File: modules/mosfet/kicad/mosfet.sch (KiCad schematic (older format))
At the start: 9 parts, among them P1 CONN_01X02, P2 CONN_01X02, P3 CONN_01X02, P4 CONN_01X02, Q1 BC547, Q2 IRF540N

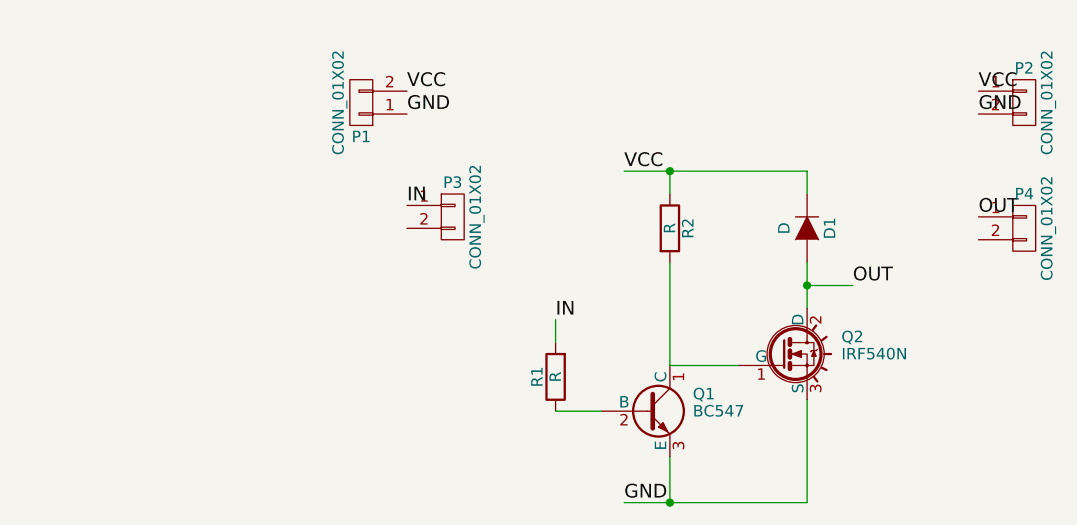
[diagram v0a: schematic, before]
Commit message: Fixes issue #1
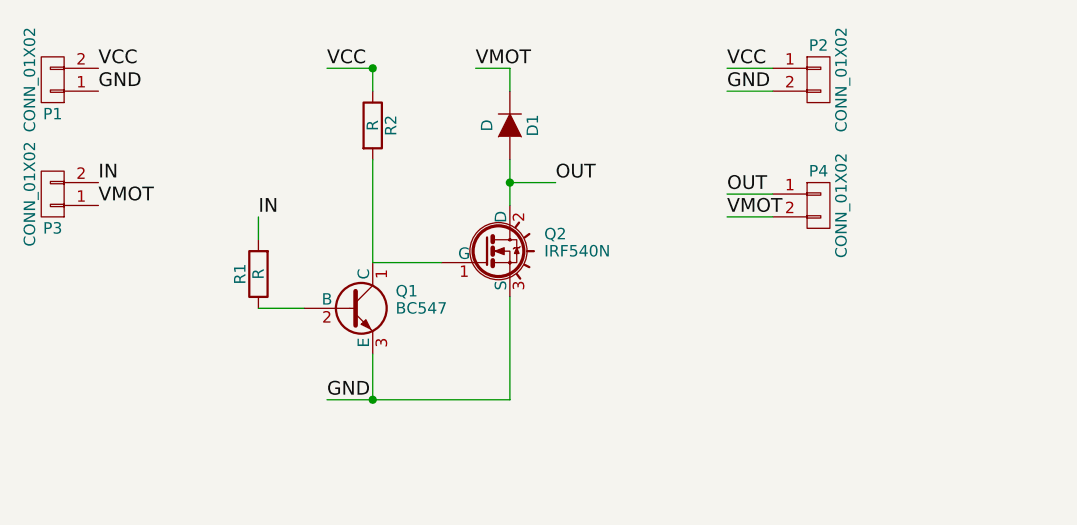
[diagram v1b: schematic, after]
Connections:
- net IN: now also P3.2 (P2); no longer P3.1 (P1)
- net VCC: no longer D1.1 (K)
- net VMOT: now reaches P4.2 (P2)
- net VMOT: now also D1.1 (K), P3.1 (P1)
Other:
- moved on the sheet: D1, P1, P2, P3, P4, Q1, Q2, R1, R2
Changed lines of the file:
@@
 LIBS:contrib
 LIBS:valves
-LIBS:modulo_mosfet-cache
+LIBS:mosfet-cache
 EELAYER 25 0
 EELAYER END
@@
 L IRF540N Q2
 U 1 1 5821F323
-P 4350 2300
-F 0 "Q2" H 4600 2375 50  0000 L CNN
-F 1 "IRF540N" H 4600 2300 50  0000 L CNN
-F 2 "TO_SOT_Packages_THT:TO-220_Neutral123_Vertical_LargePads" H 4600 2225 50  0001 L CIN
-F 3 "" H 4350 2300 50  0000 L CNN
-	1    4350 2300
+P 3050 1850
+F 0 "Q2" H 3300 1925 50  0000 L CNN
+F 1 "IRF540N" H 3300 1850 50  0000 L CNN
+F 2 "TO_SOT_Packages_THT:TO-220_Neutral123_Vertical_LargePads" H 3300 1775 50  0001 L CIN
+F 3 "" H 3050 1850 50  0000 L CNN
+	1    3050 1850
 	1    0    0    -1
 $EndComp
@@
 L BC547 Q1
 U 1 1 5821F378
-P 3750 2550
-F 0 "Q1" H 3950 2625 50  0000 L CNN
-F 1 "BC547" H 3950 2550 50  0000 L CNN
-F 2 "TO_SOT_Packages_THT:TO-92_Molded_Narrow" H 3950 2475 50  0001 L CIN
-F 3 "" H 3750 2550 50  0000 L CNN
-	1    3750 2550
+P 2450 2100
+F 0 "Q1" H 2650 2175 50  0000 L CNN
+F 1 "BC547" H 2650 2100 50  0000 L CNN
+F 2 "TO_SOT_Packages_THT:TO-92_Molded_Narrow" H 2650 2025 50  0001 L CIN
+F 3 "" H 2450 2100 50  0000 L CNN
+	1    2450 2100
 	1    0    0    -1
 $EndComp
@@
 L D D1
 U 1 1 5821F3BF
-P 4450 1750
-F 0 "D1" H 4450 1850 50  0000 C CNN
-F 1 "D" H 4450 1650 50  0000 C CNN
-F 2 "Diodes_ThroughHole:Diode_DO-35_SOD27_Horizontal_RM10" H 4450 1750 50  0001 C CNN
-F 3 "" H 4450 1750 50  0000 C CNN
-	1    4450 1750
+P 3150 1300
+F 0 "D1" H 3150 1400 50  0000 C CNN
+F 1 "D" H 3150 1200 50  0000 C CNN
+F 2 "Diodes_ThroughHole:Diode_DO-35_SOD27_Horizontal_RM10" H 3150 1300 50  0001 C CNN
+F 3 "" H 3150 1300 50  0000 C CNN
+	1    3150 1300
 	0    1    1    0
 $EndComp
@@
 L R R2
 U 1 1 5821F450
-P 3850 1750
-F 0 "R2" V 3930 1750 50  0000 C CNN
-F 1 "R" V 3850 1750 50  0000 C CNN
-F 2 "Resistors_ThroughHole:Resistor_Horizontal_RM7mm" V 3780 1750 50  0001 C CNN
-F 3 "" H 3850 1750 50  0000 C CNN
-	1    3850 1750
+P 2550 1300
+F 0 "R2" V 2630 1300 50  0000 C CNN
+F 1 "R" V 2550 1300 50  0000 C CNN
+F 2 "Resistors_ThroughHole:Resistor_Horizontal_RM7mm" V 2480 1300 50  0001 C CNN
+F 3 "" H 2550 1300 50  0000 C CNN
+	1    2550 1300
 	1    0    0    -1
 $EndComp
@@
 L R R1
 U 1 1 5821F4D9
-P 3350 2400
-F 0 "R1" V 3430 2400 50  0000 C CNN
-F 1 "R" V 3350 2400 50  0000 C CNN
-F 2 "Resistors_ThroughHole:Resistor_Horizontal_RM7mm" V 3280 2400 50  0001 C CNN
-F 3 "" H 3350 2400 50  0000 C CNN
-	1    3350 2400
+P 2050 1950
+F 0 "R1" V 2130 1950 50  0000 C CNN
+F 1 "R" V 2050 1950 50  0000 C CNN
+F 2 "Resistors_ThroughHole:Resistor_Horizontal_RM7mm" V 1980 1950 50  0001 C CNN
+F 3 "" H 2050 1950 50  0000 C CNN
+	1    2050 1950
 	-1   0    0    1
 $EndComp
@@
 L CONN_01X02 P2
 U 1 1 5821F5FC
-P 5400 1200
-F 0 "P2" H 5400 1350 50  0000 C CNN
-F 1 "CONN_01X02" V 5500 1200 50  0000 C CNN
-F 2 "Pin_Headers:Pin_Header_Angled_1x02" H 5400 1200 50  0001 C CNN
-F 3 "" H 5400 1200 50  0000 C CNN
-	1    5400 1200
+P 4500 1100
+F 0 "P2" H 4500 1250 50  0000 C CNN
+F 1 "CONN_01X02" V 4600 1100 50  0000 C CNN
+F 2 "Pin_Headers:Pin_Header_Angled_1x02" H 4500 1100 50  0001 C CNN
+F 3 "" H 4500 1100 50  0000 C CNN
+	1    4500 1100
 	1    0    0    -1
 $EndComp
-Text Label 2700 1250 0    60   ~ 0
+Text Label 1350 1150 0    60   ~ 0
 GND
-Text Label 2700 1150 0    60   ~ 0
+Text Label 1350 1050 0    60   ~ 0
 VCC
-Text Label 3650 1500 0    60   ~ 0
+Text Label 2350 1050 0    60   ~ 0
 VCC
-Text Label 3650 2950 0    60   ~ 0
+Text Label 2350 2500 0    60   ~ 0
 GND
-Text Label 5200 1150 0    60   ~ 0
+Text Label 4100 1050 0    60   ~ 0
 VCC
-Text Label 5200 1250 0    60   ~ 0
+Text Label 4100 1150 0    60   ~ 0
 GND
-Text Label 4650 2000 0    60   ~ 0
+Text Label 3350 1550 0    60   ~ 0
 OUT
-Text Label 3350 2150 0    60   ~ 0
+Text Label 2050 1700 0    60   ~ 0
 IN
-Wire Wire Line
-	3350 2550 3550 2550
-Wire Wire Line
-	3850 2350 4150 2350
-Wire Wire Line
-	3850 1900 3850 2350
-Wire Wire Line
-	3850 1600 3850 1500
-Wire Wire Line
-	4450 1500 4450 1600
-Wire Wire Line
-	4450 1900 4450 2100
-Connection ~ 3850 1500
-Wire Wire Line
-	4450 2950 4450 2500
-Wire Wire Line
-	3850 2950 3850 2750
-Connection ~ 3850 2950
-Wire Wire Line
-	4450 2000 4650 2000
-Connection ~ 4450 2000
-Wire Wire Line
-	3650 1500 4450 1500
-Wire Wire Line
-	3650 2950 4450 2950
-Wire Wire Line
-	3350 2250 3350 2150
 $Comp
 L CONN_01X02 P4
 U 1 1 5824766C
-P 5400 1750
-F 0 "P4" H 5400 1900 50  0000 C CNN
-F 1 "CONN_01X02" V 5500 1750 50  0000 C CNN
-F 2 "Pin_Headers:Pin_Header_Angled_1x02" H 5400 1750 50  0001 C CNN
-F 3 "" H 5400 1750 50  0000 C CNN
-	1    5400 1750
+P 4500 1650
+F 0 "P4" H 4500 1800 50  0000 C CNN
+F 1 "CONN_01X02" V 4600 1650 50  0000 C CNN
+F 2 "Pin_Headers:Pin_Header_Angled_1x02" H 4500 1650 50  0001 C CNN
+F 3 "" H 4500 1650 50  0000 C CNN
+	1    4500 1650
 	1    0    0    -1
 $EndComp
-Text Label 2700 1650 0    60   ~ 0
+Text Label 1350 1550 0    60   ~ 0
 IN
-Text Label 5200 1700 0    60   ~ 0
+Text Label 4100 1600 0    60   ~ 0
 OUT
 $Comp
 L CONN_01X02 P1
 U 1 1 58248EEF
-P 2500 1200
-F 0 "P1" H 2500 1350 50  0000 C CNN
-F 1 "CONN_01X02" V 2600 1200 50  0000 C CNN
-F 2 "Pin_Headers:Pin_Header_Angled_1x02" H 2500 1200 50  0001 C CNN
-F 3 "" H 2500 1200 50  0000 C CNN
-	1    2500 1200
+P 1150 1100
+F 0 "P1" H 1150 1250 50  0000 C CNN
+F 1 "CONN_01X02" V 1250 1100 50  0000 C CNN
+F 2 "Pin_Headers:Pin_Header_Angled_1x02" H 1150 1100 50  0001 C CNN
+F 3 "" H 1150 1100 50  0000 C CNN
+	1    1150 1100
 	-1   0    0    1
 $EndComp
@@
 L CONN_01X02 P3
 U 1 1 58248F49
-P 2900 1700
-F 0 "P3" H 2900 1850 50  0000 C CNN
-F 1 "CONN_01X02" V 3000 1700 50  0000 C CNN
-F 2 "Pin_Headers:Pin_Header_Angled_1x02" H 2900 1700 50  0001 C CNN
-F 3 "" H 2900 1700 50  0000 C CNN
-	1    2900 1700
-	1    0    0    -1
+P 1150 1600
+F 0 "P3" H 1150 1750 50  0000 C CNN
+F 1 "CONN_01X02" V 1250 1600 50  0000 C CNN
+F 2 "Pin_Headers:Pin_Header_Angled_1x02" H 1150 1600 50  0001 C CNN
+F 3 "" H 1150 1600 50  0000 C CNN
+	1    1150 1600
+	-1   0    0    1
 $EndComp
+Text Label 1350 1650 0    60   ~ 0
+VMOT
+Text Label 4100 1700 0    60   ~ 0
+VMOT
+Wire Wire Line
+	2050 2100 2250 2100
+Wire Wire Line
+	2550 1900 2850 1900
+Wire Wire Line
+	2550 1450 2550 1900
+Wire Wire Line
+	2550 1150 2550 1050
+Wire Wire Line
+	3150 1050 3150 1150
+Wire Wire Line
+	3150 1450 3150 1650
+Connection ~ 2550 1050
+Wire Wire Line
+	3150 2500 3150 2050
+Wire Wire Line
+	2550 2500 2550 2300
+Connection ~ 2550 2500
+Wire Wire Line
+	3150 1550 3350 1550
+Connection ~ 3150 1550
+Wire Wire Line
+	2350 2500 3150 2500
+Wire Wire Line
+	2050 1800 2050 1700
+Wire Wire Line
+	4100 1700 4300 1700
+Wire Wire Line
+	4100 1600 4300 1600
+Wire Wire Line
+	4100 1150 4300 1150
+Wire Wire Line
+	4100 1050 4300 1050
+Wire Wire Line
+	2550 1050 2350 1050
+Wire Wire Line
+	3150 1050 3000 1050
+Text Label 3000 1050 0    60   ~ 0
+VMOT
 $EndSCHEMATC
